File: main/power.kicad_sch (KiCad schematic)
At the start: 14 parts, among them J5 Battery, Q2 IRLML6402, SW2 EG1215AA, U5 TLV75733PDBV

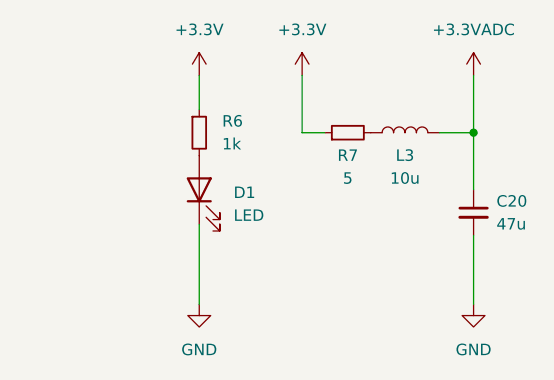
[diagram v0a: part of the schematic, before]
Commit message: feat: update main board
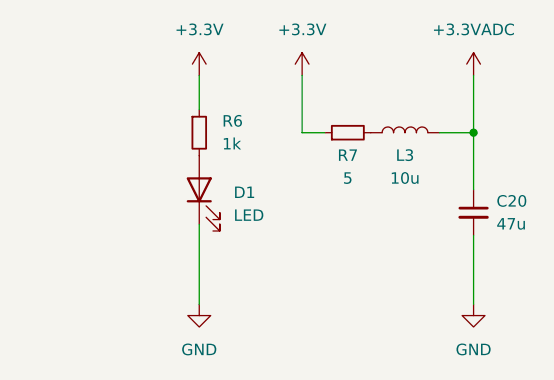
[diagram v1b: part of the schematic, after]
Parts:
- R7: footprint Resistor_SMD:R_0201_0603Metric -> Resistor_SMD:R_0805_2012Metric
